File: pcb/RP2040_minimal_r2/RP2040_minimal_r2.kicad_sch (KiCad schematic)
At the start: 34 parts, among them J2 Conn_01x02, J3 USB_C_Receptacle, SW1 DDR_North, SW2 DDR_South, SW3 DDR_East, SW4 DDR_West, U1 NCP1117-3.3_SOT223, U2 W25Q128JVS, U3 RP2040, Y1 ABM8-272-T3

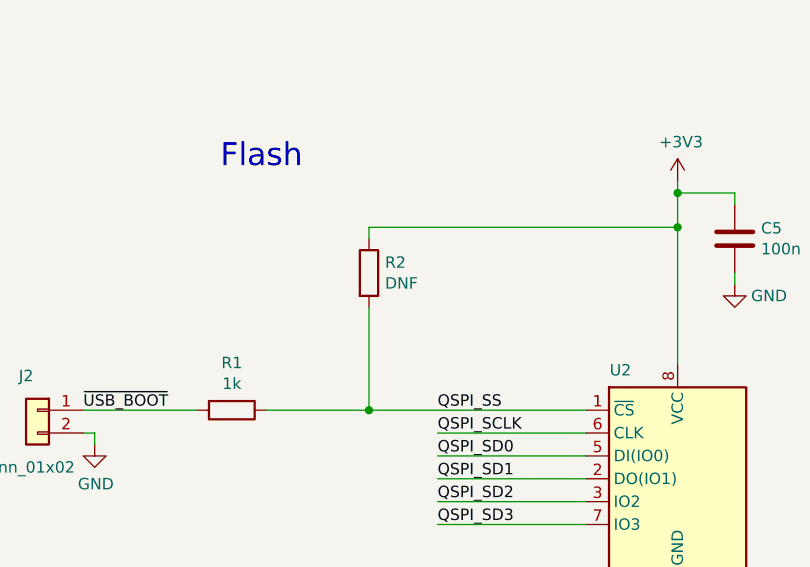
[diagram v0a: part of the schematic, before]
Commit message: add rest of lcsc numbers
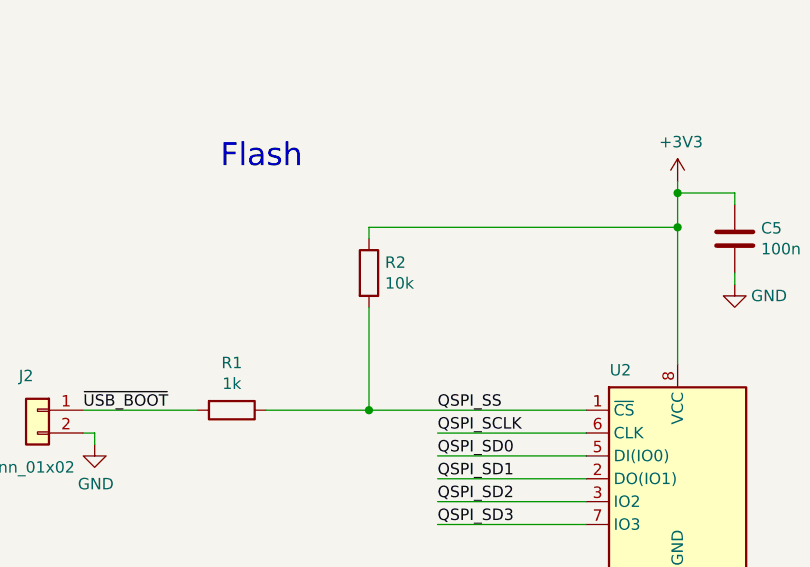
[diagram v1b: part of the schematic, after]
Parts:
- C1, C17, C4: LCSC (none) -> C440198
- C10, C8: LCSC (none) -> C29266
- C11, C12, C13, C14, C15, C16, C5, C6, C7, C9: LCSC (none) -> C60474
- C2, C3: LCSC (none) -> C86285
- J3: LCSC (none) -> C2765186
- R1, R5: LCSC (none) -> C106235
- R2: value DNF -> 10k; LCSC (none) -> C60490
- R3, R4: LCSC (none) -> C138021
- R6, R7: LCSC (none) -> C105872
- U1: LCSC (none) -> C26537
- U2: LCSC (none) -> C113767
- U3: LCSC (none) -> C2040
- Y1: LCSC (none) -> C20625731
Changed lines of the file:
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@@
 			)
 		)
-		(property "LCSC" ""
+		(property "LCSC" "C2040"
 			(at 198.12 144.78 0)
 			(hide yes)
@@
 			)
 		)
-		(property "LCSC" ""
+		(property "LCSC" "C113767"
 			(at 102.87 193.675 0)
 			(hide yes)
@@
 			)
 		)
-		(property "Value" "DNF"
+		(property "Value" "10k"
 			(at 70.358 171.958 0)
 			(show_name no)
@@
 			)
 		)
-		(property "LCSC" ""
+		(property "LCSC" "C60490"
 			(at 68.58 170.815 0)
 			(hide yes)
@@
 			)
 		)
-		(property "LCSC" ""
+		(property "LCSC" "C106235"
 			(at 53.34 186.055 90)
 			(hide yes)
@@
 			)
 		)
-		(property "LCSC" ""
+		(property "LCSC" "C60474"
 			(at 109.22 167.005 0)
 			(hide yes)
@@
 			)
 		)
-		(property "LCSC" ""
+		(property "LCSC" "C138021"
 			(at 245.11 96.52 90)
 			(hide yes)
@@
 			)
 		)
-		(property "LCSC" ""
+		(property "LCSC" "C138021"
 			(at 245.11 104.14 90)
 			(hide yes)
@@
 			)
 		)
-		(property "LCSC" ""
+		(property "LCSC" "C60474"
 			(at 223.52 66.04 0)
 			(hide yes)
@@
 			)
 		)
-		(property "LCSC" ""
+		(property "LCSC" "C60474"
 			(at 234.95 66.04 0)
 			(hide yes)
@@
 			)
 		)
-		(property "LCSC" ""
+		(property "LCSC" "C60474"
 			(at 246.38 66.04 0)
 			(hide yes)
@@
 			)
 		)
-		(property "LCSC" ""
+		(property "LCSC" "C60474"
 			(at 257.81 66.04 0)
 			(hide yes)
@@
 			)
 		)
-		(property "LCSC" ""
+		(property "LCSC" "C60474"
 			(at 269.24 66.04 0)
 			(hide yes)
@@
 			)
 		)
-		(property "LCSC" ""
+		(property "LCSC" "C60474"
 			(at 280.67 66.04 0)
 			(hide yes)
@@
 			)
 		)
-		(property "LCSC" ""
+		(property "LCSC" "C60474"
 			(at 292.1 66.04 0)
 			(hide yes)
@@
 			)
 		)
-		(property "LCSC" ""
+		(property "LCSC" "C60474"
 			(at 157.48 66.04 0)
 			(hide yes)
@@
 			)
 		)
-		(property "LCSC" ""
+		(property "LCSC" "C60474"
 			(at 168.91 66.04 0)
 			(hide yes)
@@
 			)
 		)
-		(property "LCSC" ""
+		(property "LCSC" "C29266"
 			(at 168.91 81.28 0)
 			(hide yes)
@@
 			)
 		)
-		(property "LCSC" ""
+		(property "LCSC" "C29266"
 			(at 223.52 81.28 0)
 			(hide yes)
@@
 			)
 		)
-		(property "LCSC" ""
+		(property "LCSC" "C26537"
 			(at 97.79 52.07 0)
 			(hide yes)
@@
 			)
 		)
-		(property "LCSC" ""
+		(property "LCSC" "C440198"
 			(at 80.01 57.15 0)
 			(hide yes)
@@
 			)
 		)
-		(property "LCSC" ""
+		(property "LCSC" "C440198"
 			(at 115.57 57.15 0)
 			(hide yes)
@@
 			)
 		)
-		(property "LCSC" ""
+		(property "LCSC" "C440198"
 			(at 351.79 193.04 0)
 			(hide yes)
@@
 			)
 		)
-		(property "LCSC" ""
+		(property "LCSC" "C105872"
 			(at 68.58 71.12 90)
 			(hide yes)
@@
 			)
 		)
-		(property "LCSC" ""
+		(property "LCSC" "C20625731"
 			(at 62.23 242.57 90)
 			(hide yes)
@@
 			)
 		)
-		(property "LCSC" ""
+		(property "LCSC" "C86285"
 			(at 46.99 237.49 0)
 			(hide yes)
@@
 			)
 		)
-		(property "LCSC" ""
+		(property "LCSC" "C2765186"
 			(at 46.99 88.9 0)
 			(hide yes)
@@
 			)
 		)
-		(property "LCSC" ""
+		(property "LCSC" "C106235"
 			(at 80.01 247.65 90)
 			(hide yes)
@@
 			)
 		)
-		(property "LCSC" ""
+		(property "LCSC" "C86285"
 			(at 46.99 247.65 0)
 			(hide yes)
@@
 			)
 		)
-		(property "LCSC" ""
+		(property "LCSC" "C105872"
 			(at 68.58 68.58 90)
 			(hide yes)
